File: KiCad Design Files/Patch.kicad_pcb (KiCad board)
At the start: 2 copper layers, 47 x 47 mm, 1 part, among them J1 RF Connector

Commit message: Patch antenna design transfer finished. Screws to be added
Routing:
- added copper zone on F.Cu, net /RF_COPPER
- removed copper zone on F.Cu, net (none)
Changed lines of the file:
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@@
     (descr "solder Pin_ diameter 1.0mm, hole diameter 1.0mm (press fit), length 10.0mm")
     (tags "solder Pin_ press fit")
+    (clearance 1)
     (fp_text reference J1 (at 0 2.25) (layer F.SilkS)
       (effects (font (size 1 1) (thickness 0.15)))
@@
       (effects (font (size 1 1) (thickness 0.15)))
     )
+    (fp_circle (center 0 0) (end 1.25 0.05) (layer F.SilkS) (width 0.12))
+    (fp_circle (center 0 0) (end 1 0) (layer F.Fab) (width 0.12))
+    (fp_circle (center 0 0) (end 0.5 0) (layer F.Fab) (width 0.12))
+    (fp_circle (center 0 0) (end 1.5 0) (layer F.CrtYd) (width 0.05))
     (fp_text user %R (at 0 2.25) (layer F.Fab)
       (effects (font (size 1 1) (thickness 0.15)))
     )
-    (fp_circle (center 0 0) (end 1.5 0) (layer F.CrtYd) (width 0.05))
-    (fp_circle (center 0 0) (end 0.5 0) (layer F.Fab) (width 0.12))
-    (fp_circle (center 0 0) (end 1 0) (layer F.Fab) (width 0.12))
-    (fp_circle (center 0 0) (end 1.25 0.05) (layer F.SilkS) (width 0.12))
     (pad 1 thru_hole circle (at 0 0) (size 3 3) (drill 2) (layers *.Cu *.Mask)
       (net 1 /RF_COPPER))
@@
     )
   )
-  (zone (net 0) (net_name "") (layer Top) (hatch edge 0.508)
+  (zone (net 1) (net_name /RF_COPPER) (layer Top) (hatch edge 0.508)
     (priority 6)
     (connect_pads (clearance 0.000001))
     (min_thickness 0.0254)
-    (fill (arc_segments 32) (thermal_gap 0.051) (thermal_bridge_width 0.051))
+    (fill yes (arc_segments 32) (thermal_gap 0.051) (thermal_bridge_width 0.051))
     (polygon
       (pts
@@
     (connect_pads (clearance 0.000001))
     (min_thickness 0.0254)
-    (fill (arc_segments 32) (thermal_gap 0.051) (thermal_bridge_width 0.051))
+    (fill yes (arc_segments 32) (thermal_gap 0.051) (thermal_bridge_width 0.051))
     (polygon
       (pts

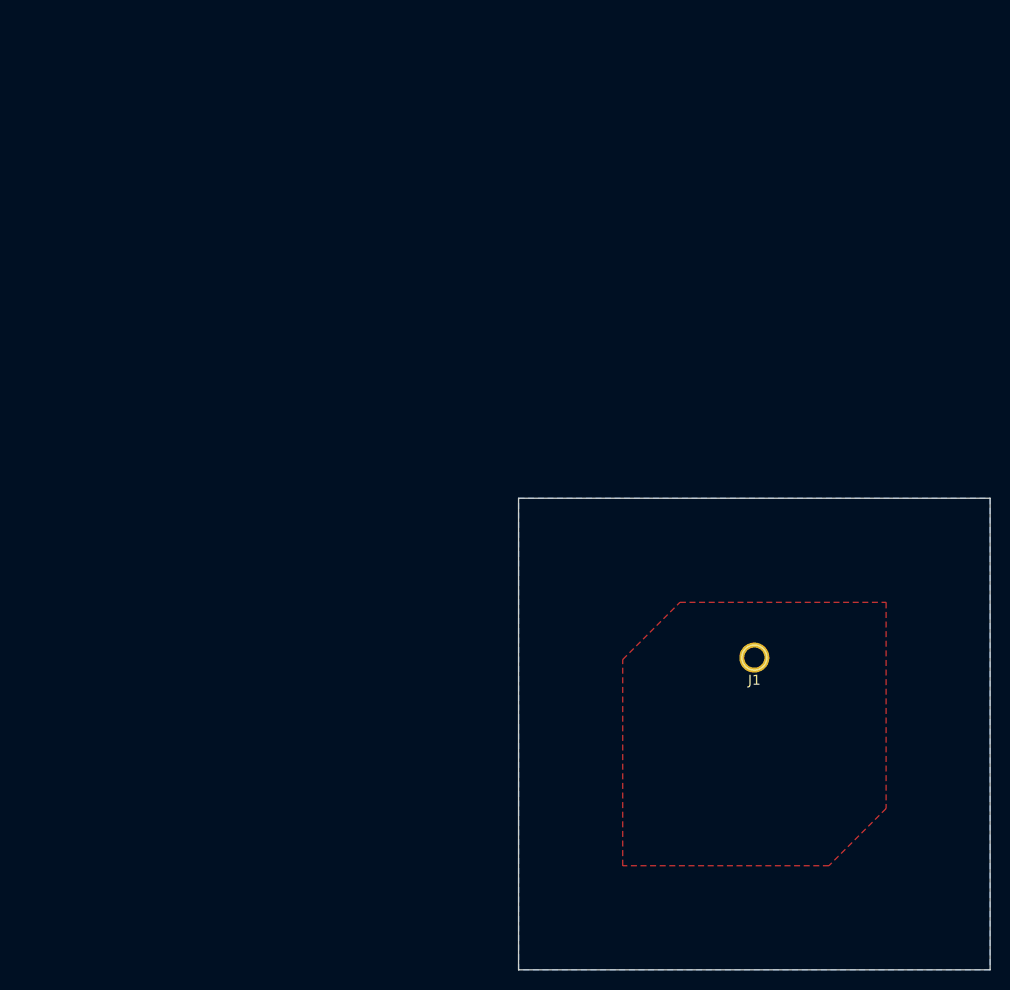
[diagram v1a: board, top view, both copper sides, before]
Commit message: Added screws to the antenna
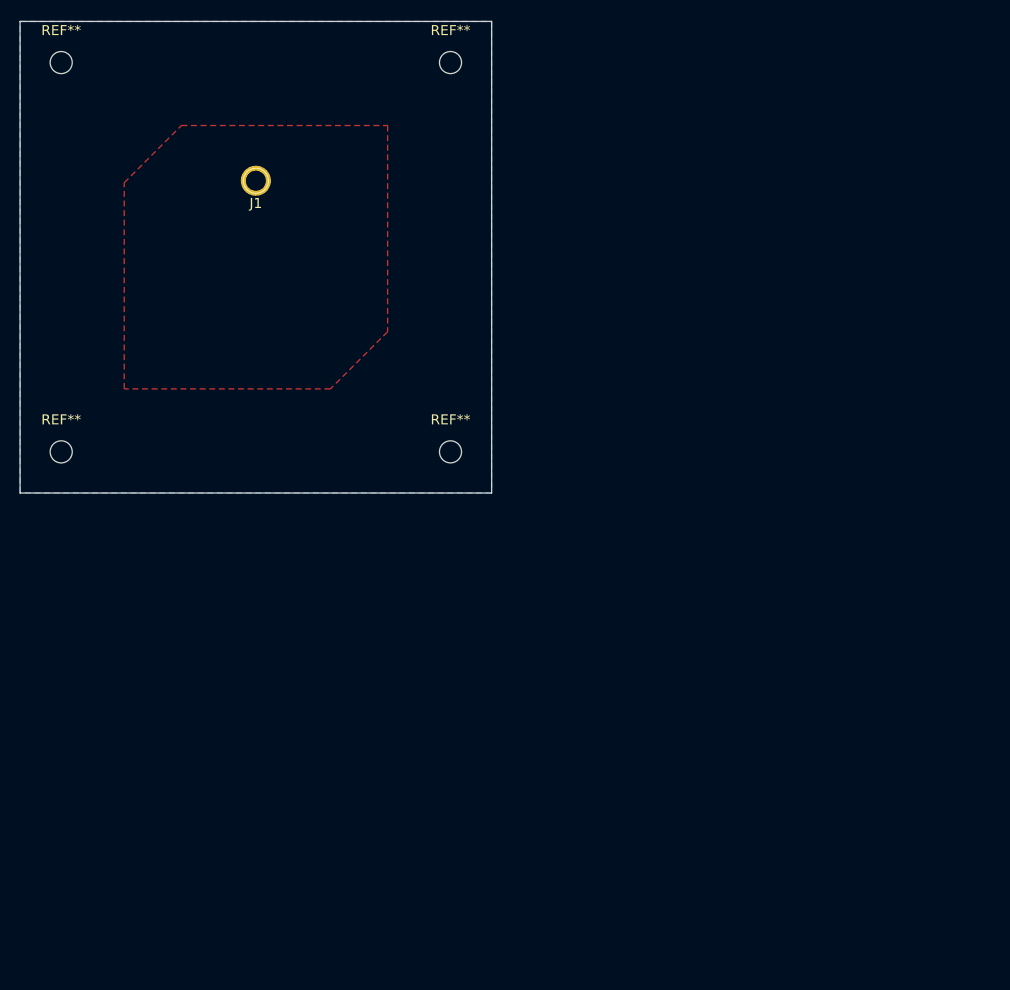
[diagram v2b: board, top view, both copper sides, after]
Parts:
- added REF**: MountingHole_2.2mm_M2, MountingHole:MountingHole_2.2mm_M2, F.Cu at (118.2, 76.9)
- added REF**: MountingHole_2.2mm_M2, MountingHole:MountingHole_2.2mm_M2, F.Cu at (118.2, 38.1)
- added REF**: MountingHole_2.2mm_M2, MountingHole:MountingHole_2.2mm_M2, F.Cu at (79.4, 76.9)
- added REF**: MountingHole_2.2mm_M2, MountingHole:MountingHole_2.2mm_M2, F.Cu at (79.4, 38.1)
- moved J1 68.8 mm to (98.8, 49.9)
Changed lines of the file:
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@@
     (tracks 0)
     (zones 0)
-    (modules 1)
+    (modules 5)
     (nets 2)
   )
-  (page A4)
+  (page User 210.007 148.006)
+  (title_block
+    (title "2.4GHz Patch Antenna")
+    (date 2020-09-11)
+    (rev v1.0)
+    (company "Asristotle Space & Aeronautics Team (ASAT)")
+    (comment 1 AcubeSAT)
+  )
   (layers
     (0 Top signal)
@@
     (mod_text_size 1 1)
     (mod_text_width 0.15)
-    (pad_size 3 3)
-    (pad_drill 2)
+    (pad_size 2.2 2.2)
+    (pad_drill 2.2)
     (pad_to_mask_clearance 0.05)
     (aux_axis_origin 0 0)
@@
     (add_net /RF_COPPER)
   )
+  (module MountingHole:MountingHole_2.2mm_M2 (layer Top)
+    (at 118.2187 76.8802)
+    (descr "Mounting Hole 2.2mm, no annular, M2")
+    (tags "mounting hole 2.2mm no annular m2")
+    (attr virtual)
+    (fp_text reference REF** (at 0 -3.2) (layer F.SilkS)
+      (effects (font (size 1 1) (thickness 0.15)))
+    )
+    (fp_text value MountingHole_2.2mm_M2 (at 0 3.2) (layer F.Fab)
+      (effects (font (size 1 1) (thickness 0.15)))
+    )
+    (fp_circle (center 0 0) (end 2.2 0) (layer Cmts.User) (width 0.15))
+    (fp_circle (center 0 0) (end 2.45 0) (layer F.CrtYd) (width 0.05))
+    (fp_text user %R (at 0.3 0) (layer F.Fab)
+      (effects (font (size 1 1) (thickness 0.15)))
+    )
+    (pad "" np_thru_hole circle (at 0 0) (size 2.2 2.2) (drill 2.2) (layers *.Cu *.Mask)
+      (clearance 0.5))
+  )
+  (module MountingHole:MountingHole_2.2mm_M2 (layer Top)
+    (at 118.2187 38.0802)
+    (descr "Mounting Hole 2.2mm, no annular, M2")
+    (tags "mounting hole 2.2mm no annular m2")
+    (attr virtual)
+    (fp_text reference REF** (at 0 -3.2) (layer F.SilkS)
+      (effects (font (size 1 1) (thickness 0.15)))
+    )
+    (fp_text value MountingHole_2.2mm_M2 (at 0 3.2) (layer F.Fab)
+      (effects (font (size 1 1) (thickness 0.15)))
+    )
+    (fp_circle (center 0 0) (end 2.2 0) (layer Cmts.User) (width 0.15))
+    (fp_circle (center 0 0) (end 2.45 0) (layer F.CrtYd) (width 0.05))
+    (fp_text user %R (at 0.3 0) (layer F.Fab)
+      (effects (font (size 1 1) (thickness 0.15)))
+    )
+    (pad "" np_thru_hole circle (at 0 0) (size 2.2 2.2) (drill 2.2) (layers *.Cu *.Mask)
+      (clearance 0.5))
+  )
+  (module MountingHole:MountingHole_2.2mm_M2 (layer Top)
+    (at 79.4187 76.8802)
+    (descr "Mounting Hole 2.2mm, no annular, M2")
+    (tags "mounting hole 2.2mm no annular m2")
+    (attr virtual)
+    (fp_text reference REF** (at 0 -3.2) (layer F.SilkS)
+      (effects (font (size 1 1) (thickness 0.15)))
+    )
+    (fp_text value MountingHole_2.2mm_M2 (at 0 3.2) (layer F.Fab)
+      (effects (font (size 1 1) (thickness 0.15)))
+    )
+    (fp_circle (center 0 0) (end 2.2 0) (layer Cmts.User) (width 0.15))
+    (fp_circle (center 0 0) (end 2.45 0) (layer F.CrtYd) (width 0.05))
+    (fp_text user %R (at 0.3 0) (layer F.Fab)
+      (effects (font (size 1 1) (thickness 0.15)))
+    )
+    (pad "" np_thru_hole circle (at 0 0) (size 2.2 2.2) (drill 2.2) (layers *.Cu *.Mask)
+      (clearance 0.5))
+  )
+  (module MountingHole:MountingHole_2.2mm_M2 (layer Top)
+    (at 79.4187 38.0802)
+    (descr "Mounting Hole 2.2mm, no annular, M2")
+    (tags "mounting hole 2.2mm no annular m2")
+    (attr virtual)
+    (fp_text reference REF** (at 0 -3.2) (layer F.SilkS)
+      (effects (font (size 1 1) (thickness 0.15)))
+    )
+    (fp_text value MountingHole_2.2mm_M2 (at 0 3.2) (layer F.Fab)
+      (effects (font (size 1 1) (thickness 0.15)))
+    )
+    (fp_text user %R (at 0.3 0) (layer F.Fab)
+      (effects (font (size 1 1) (thickness 0.15)))
+    )
+    (fp_circle (center 0 0) (end 2.2 0) (layer Cmts.User) (width 0.15))
+    (fp_circle (center 0 0) (end 2.45 0) (layer F.CrtYd) (width 0.05))
+    (pad "" np_thru_hole circle (at 0 0) (size 2.2 2.2) (drill 2.2) (layers *.Cu *.Mask)
+      (clearance 0.5))
+  )
   (module Connector_Pin:Pin_D1.0mm_L10.0mm (layer Top)
-    (at 148.5011 97.3836)
+    (at 98.8187 49.8602)
     (descr "solder Pin_ diameter 1.0mm, hole diameter 1.0mm (press fit), length 10.0mm")
     (tags "solder Pin_ press fit")
@@
       (effects (font (size 1 1) (thickness 0.15)))
     )
+    (fp_circle (center 0 0) (end 1.5 0) (layer F.CrtYd) (width 0.05))
+    (fp_circle (center 0 0) (end 0.5 0) (layer F.Fab) (width 0.12))
+    (fp_circle (center 0 0) (end 1 0) (layer F.Fab) (width 0.12))
     (fp_circle (center 0 0) (end 1.25 0.05) (layer F.SilkS) (width 0.12))
-    (fp_circle (center 0 0) (end 1 0) (layer F.Fab) (width 0.12))
-    (fp_circle (center 0 0) (end 0.5 0) (layer F.Fab) (width 0.12))
-    (fp_circle (center 0 0) (end 1.5 0) (layer F.CrtYd) (width 0.05))
     (fp_text user %R (at 0 2.25) (layer F.Fab)
       (effects (font (size 1 1) (thickness 0.15)))
@@
     )
   )
-  (gr_line (start 172.0011 128.5036) (end 172.0011 81.5036) (layer Edge.Cuts) (width 0.001))
-  (gr_line (start 172.0011 81.5036) (end 125.0011 81.5036) (layer Edge.Cuts) (width 0.001))
-  (gr_line (start 125.0011 81.5036) (end 125.0011 128.5036) (layer Edge.Cuts) (width 0.001))
-  (gr_line (start 125.0011 128.5036) (end 172.0011 128.5036) (layer Edge.Cuts) (width 0.001))
+  (gr_line (start 122.3187 80.9802) (end 122.3187 33.9802) (layer Edge.Cuts) (width 0.001))
+  (gr_line (start 122.3187 33.9802) (end 75.3187 33.9802) (layer Edge.Cuts) (width 0.001))
+  (gr_line (start 75.3187 33.9802) (end 75.3187 80.9802) (layer Edge.Cuts) (width 0.001))
+  (gr_line (start 75.3187 80.9802) (end 122.3187 80.9802) (layer Edge.Cuts) (width 0.001))
   (zone (net 0) (net_name "") (layer Top) (hatch edge 0.508)
     (priority 6)
@@
     (polygon
       (pts
-        (xy 143.5076 112.1981) (xy 153.5066 112.1981) (xy 153.5066 107.6981) (xy 155.0076 107.6981) (xy 155.0076 113.6991)
-        (xy 142.0066 113.6991) (xy 142.0066 107.6981) (xy 143.5076 107.6981)
+        (xy 93.8252 64.6747) (xy 103.8242 64.6747) (xy 103.8242 60.1747) (xy 105.3252 60.1747) (xy 105.3252 66.1757)
+        (xy 92.3242 66.1757) (xy 92.3242 60.1747) (xy 93.8252 60.1747)
       )
     )
@@
     (polygon
       (pts
-        (xy 161.6326 112.428807) (xy 155.932307 118.1291) (xy 135.3816 118.1291) (xy 135.3816 97.578393) (xy 141.081893 91.8781)
-        (xy 161.6326 91.8781)
+        (xy 111.9502 64.905407) (xy 106.249907 70.6057) (xy 85.6992 70.6057) (xy 85.6992 50.054993) (xy 91.399493 44.3547)
+        (xy 111.9502 44.3547)
       )
     )
@@
     (polygon
       (pts
-        (xy 171.9966 128.4991) (xy 125.0056 128.4991) (xy 125.0056 81.5081) (xy 171.9966 81.5081)
+        (xy 122.3142 80.9757) (xy 75.3232 80.9757) (xy 75.3232 33.9847) (xy 122.3142 33.9847)
       )
     )
